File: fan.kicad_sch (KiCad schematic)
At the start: 10 parts, among them J2 Conn_01x02, J4 Conn_01x04, U7 EMC2101

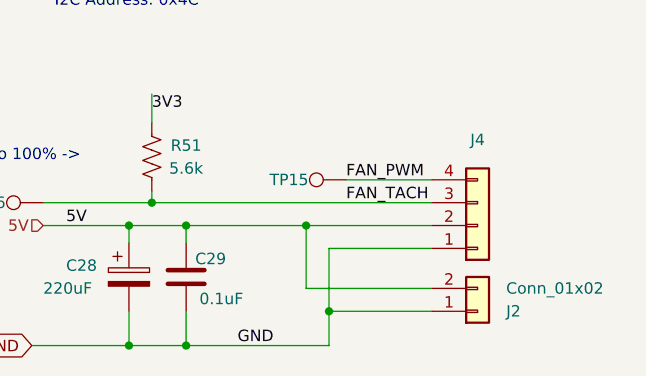
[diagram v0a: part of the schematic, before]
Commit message: Power analysis; updates to 205pd
Started analysis based on the 204 with an architecture diagram and with an smath document. Copied over manually changes from the 205 branch and started updating the schematic with USB PD capabilities. Only added decoy USB PD chip (CH224K), still need to fix power supplies.
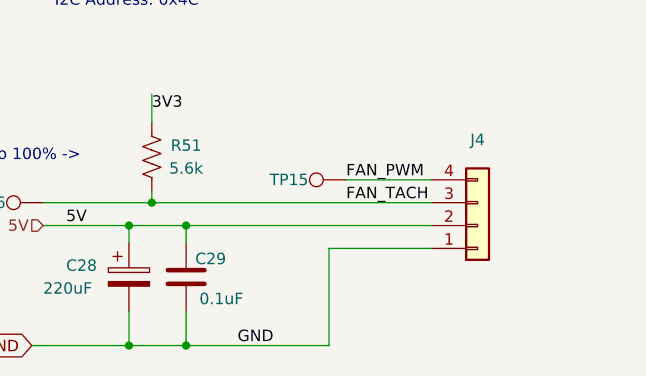
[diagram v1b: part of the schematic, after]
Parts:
- removed J2: Conn_01x02, bitaxe:JST_XH_B2B-XH-A_1x02_P2.50mm_Vertical, symbol Connector_Generic:Conn_01x02
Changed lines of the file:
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@@
   (title_block
     (title "Bitaxe Ultra")
-    (date "2023-12-10")
-    (rev "204")
+    (date "2023-12-15")
+    (rev "205")
   )
   (junction (at 191.77 66.04) (diameter 0) (color 0 0 0 0)
   )
-  (junction (at 164.465 113.665) (diameter 0) (color 0 0 0 0)
-  )
   (junction (at 151.13 113.665) (diameter 0) (color 0 0 0 0)
-  )
-  (junction (at 167.005 123.19) (diameter 0) (color 0 0 0 0)
   )
   (junction (at 147.32 111.125) (diameter 0) (color 0 0 0 0)
@@
     (stroke (width 0) (type default))
   )
-  (wire (pts (xy 164.465 120.65) (xy 178.435 120.65))
-    (stroke (width 0) (type default))
-  )
-  (wire (pts (xy 167.005 116.205) (xy 167.005 123.19))
-    (stroke (width 0) (type default))
-  )
   (wire (pts (xy 125.095 73.025) (xy 132.08 73.025))
     (stroke (width 0) (type default))
   )
-  (wire (pts (xy 167.005 123.19) (xy 167.005 127))
-    (stroke (width 0) (type default))
-  )
-  (wire (pts (xy 167.005 123.19) (xy 178.435 123.19))
+  (wire (pts (xy 167.005 116.205) (xy 167.005 127))
     (stroke (width 0) (type default))
   )
@@
     (stroke (width 0) (type default))
   )
-  (wire (pts (xy 164.465 113.665) (xy 178.435 113.665))
+  (wire (pts (xy 151.13 113.665) (xy 178.435 113.665))
     (stroke (width 0) (type default))
   )
@@
     (stroke (width 0) (type default))
   )
-  (wire (pts (xy 151.13 113.665) (xy 164.465 113.665))
-    (stroke (width 0) (type default))
-  )
   (wire (pts (xy 157.48 83.185) (xy 191.77 83.185))
     (stroke (width 0) (type default))
@@
   )
   (wire (pts (xy 133.985 127) (xy 144.78 127))
-    (stroke (width 0) (type default))
-  )
-  (wire (pts (xy 164.465 120.65) (xy 164.465 113.665))
     (stroke (width 0) (type default))
   )
@@
         )
       )
-    )
-  )
-  (symbol (lib_id "Connector_Generic:Conn_01x02") (at 183.515 123.19 0) (mirror x) (unit 1)
-    (in_bom yes) (on_board yes) (dnp no)
-    (property "Reference" "J2" (at 186.69 123.19 0)
-      (effects (font (size 1.27 1.27)) (justify left))
-    )
-    (property "Value" "Conn_01x02" (at 186.69 120.65 0)
-      (effects (font (size 1.27 1.27)) (justify left))
-    )
-    (property "Footprint" "bitaxe:JST_XH_B2B-XH-A_1x02_P2.50mm_Vertical" (at 183.515 123.19 0)
-      (effects (font (size 1.27 1.27)) hide)
-    )
-    (property "Datasheet" "https://www.jst-mfg.com/product/pdf/eng/eXH.pdf" (at 183.515 123.19 0)
-      (effects (font (size 1.27 1.27)) hide)
-    )
-    (property "DK" "455-B2B-XH-A-ND" (at 183.515 123.19 0)
-      (effects (font (size 1.27 1.27)) hide)
-    )
-    (property "PARTNO" "B2B-XH-A" (at 183.515 123.19 0)
-      (effects (font (size 1.27 1.27)) hide)
-    )
-    (pin "1")
-    (pin "2")
-    (instances
-      (project "bitaxeUltra"
-        (path "/e63e39d7-6ac0-4ffd-8aa3-1841a4541b55/8e8832ea-6bf1-49d2-b3a5-32a207f555d2"
-          (reference "J2") (unit 1)
-        )
-      )

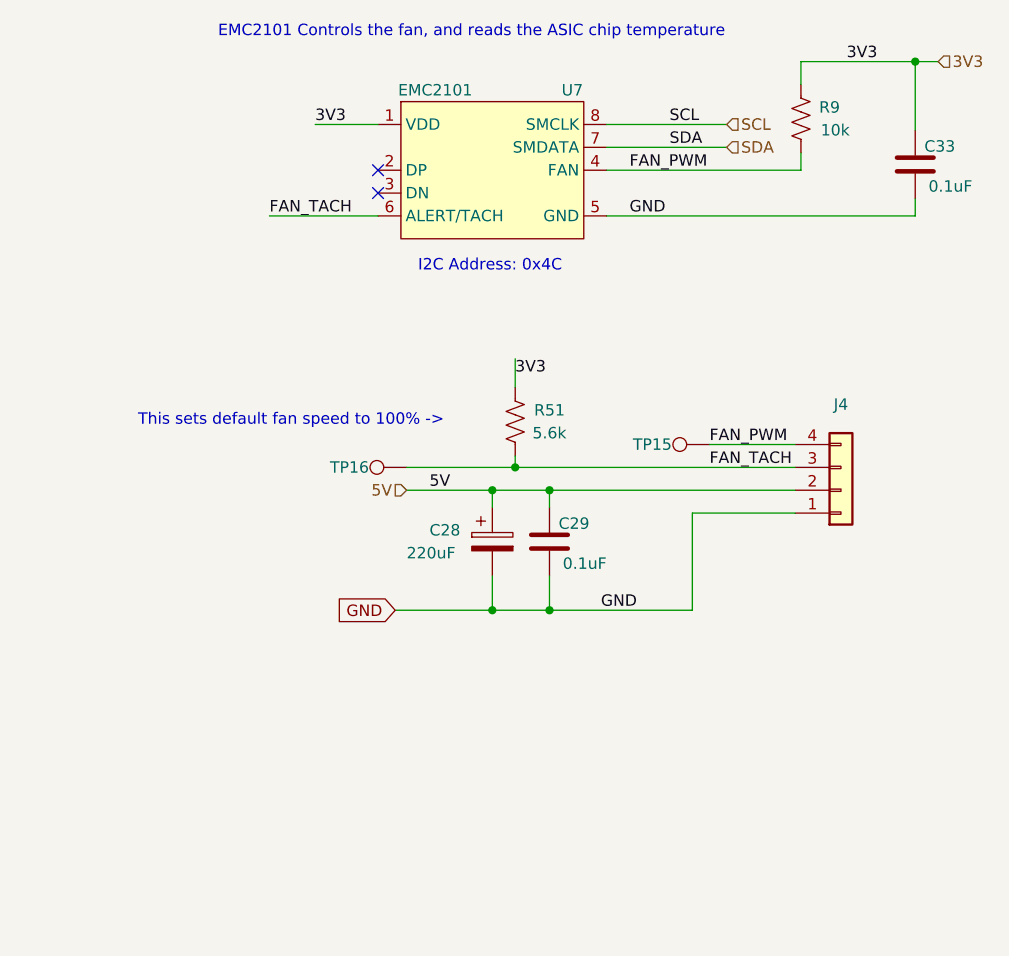
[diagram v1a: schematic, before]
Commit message: Worked on VDD
Started importing SiC431A for VDD supply. Yet to do Vfb, Mode, Pgood, boot, phase, en. Moved power supplies to power page. Configured CH224K to 12V
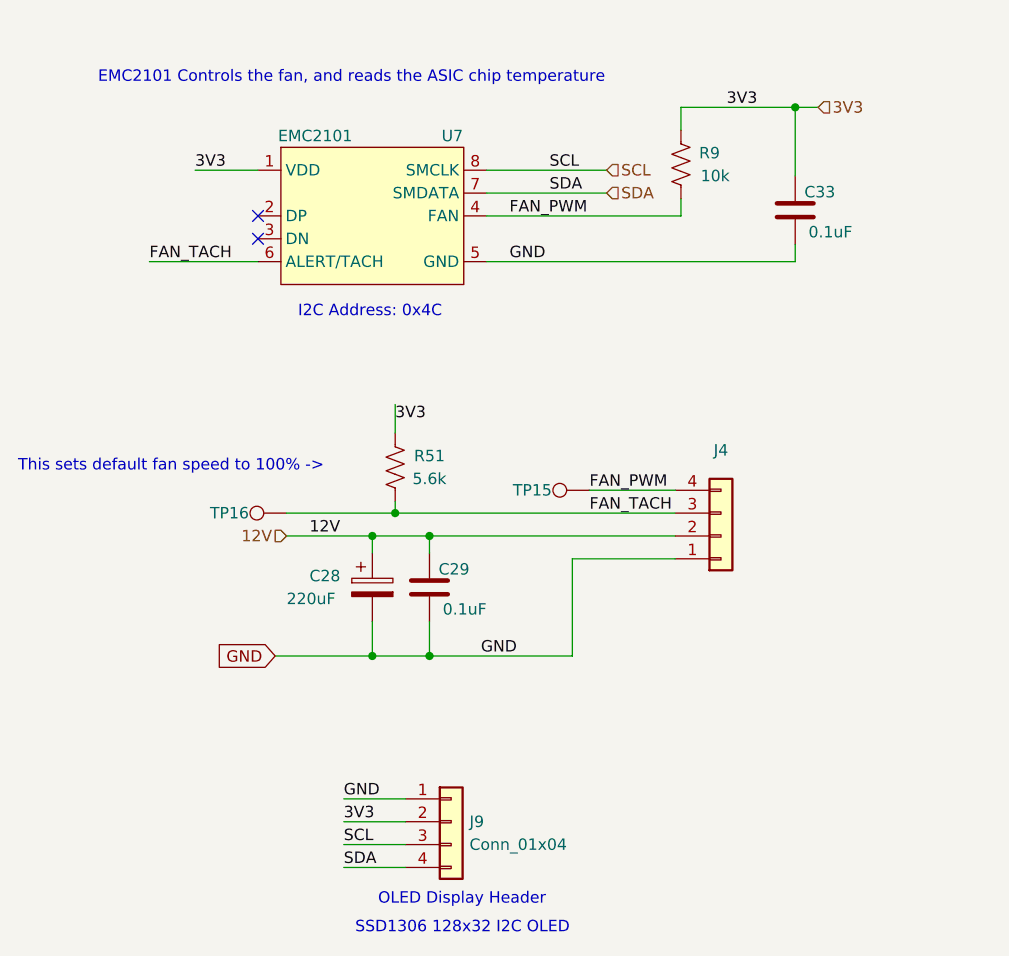
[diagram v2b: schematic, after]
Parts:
- added J9: Conn_01x04, bitaxe:PinHeader_1x04_P2.54mm_Vertical_shifted, symbol Connector_Generic:Conn_01x04
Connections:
- net 3V3: now also J9.2 (Pin_2)
- net GND: now also J9.1 (Pin_1)
- net SCL: now also J9.3 (Pin_3)
- net SDA: now also J9.4 (Pin_4)
- net 5V renamed 12V
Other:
- note added: "OLED Display Header"
- note added: "SSD1306 128x32 I2C OLED"
- moved on the sheet: C28, C29, C33, J4, R51, R9, TP15, TP16, U7

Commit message: SCH Draft 3, PCB Start
Finished some last minute changes to change 1V8 to 1V2 based on discord feedback. Updated level shifter and moved 25MHz oscillator to use 3V3 and be shifted down. Started working on layout.
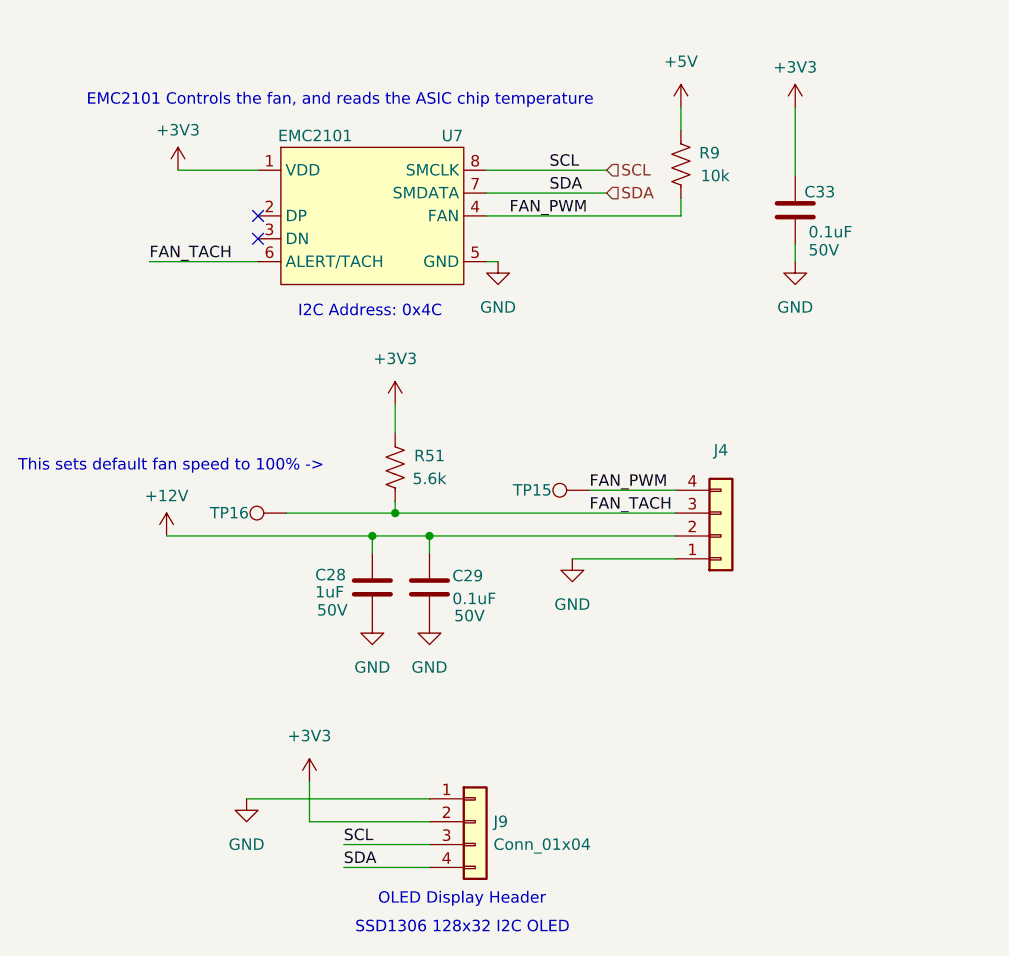
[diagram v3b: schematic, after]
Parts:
- removed C28: 220uF, Capacitor_SMD:CP_Elec_6.3x7.7, symbol Device:C_Polarized
- added C28: 1uF, Capacitor_SMD:C_0603_1608Metric, symbol Device:C
- C29, C33: DK 1292-1639-1-ND -> 490-13342-1-ND; PARTNO 0402X104K100CT -> GRM155R71H104KE14J; Voltage (none) -> 50V
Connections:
- net GND: now also C28.2
- net 12V renamed +12V
- net +12V: now also C28.1
- net 3V3 renamed +3V3
- net +3V3: no longer R9.2
- new net +5V: R9.2
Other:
- moved on the sheet: J9

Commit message: 3.3V net fix, PCB progress
Fixed accidental use of both 3V3 and 3.3V to just use 3V3. Worked on PCB
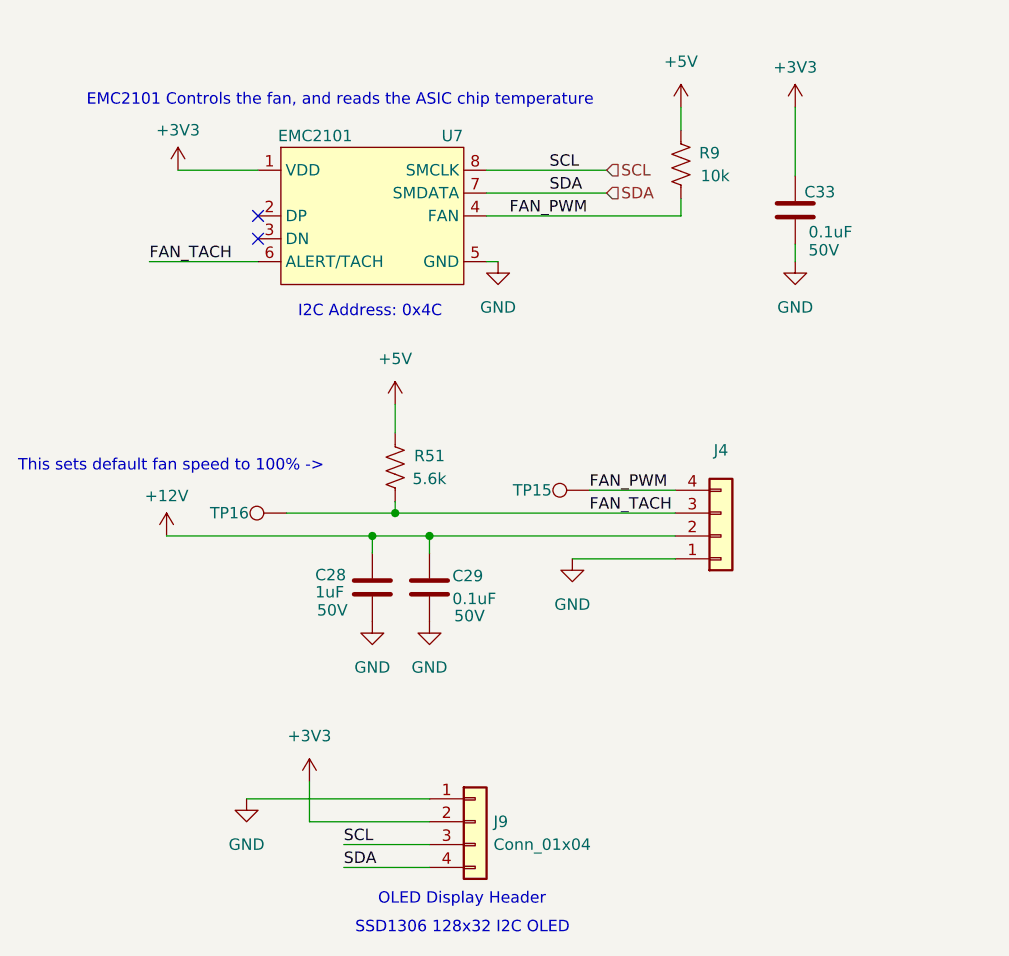
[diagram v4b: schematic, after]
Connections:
- net +3V3: no longer R51.2
- net +5V: now also R51.2
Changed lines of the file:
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@@
+    )
+  )
+  (symbol (lib_id "power:+5V") (at 133.985 104.14 0) (unit 1)
+    (in_bom yes) (on_board yes) (dnp no) (fields_autoplaced)
+    (property "Reference" "#PWR073" (at 133.985 107.95 0)
+      (effects (font (size 1.27 1.27)) hide)
+    )
+    (property "Value" "+5V" (at 133.985 99.06 0)
+      (effects (font (size 1.27 1.27)))
+    )
+    (property "Footprint" "" (at 133.985 104.14 0)
+      (effects (font (size 1.27 1.27)) hide)
+    )
+    (property "Datasheet" "" (at 133.985 104.14 0)
+      (effects (font (size 1.27 1.27)) hide)
+    )
+    (pin "1")
+    (instances
+      (project "bitaxeUltra"
+        (path "/e63e39d7-6ac0-4ffd-8aa3-1841a4541b55/8e8832ea-6bf1-49d2-b3a5-32a207f555d2"
+          (reference "#PWR073") (unit 1)
+        )
+      )
     )
   )
@@
         )
       )
-    )
-  )
-  (symbol (lib_id "power:+3V3") (at 133.985 104.14 0) (unit 1)
-    (in_bom yes) (on_board yes) (dnp no) (fields_autoplaced)
-    (property "Reference" "#PWR073" (at 133.985 107.95 0)
-      (effects (font (size 1.27 1.27)) hide)
-    )
-    (property "Value" "+3V3" (at 133.985 99.06 0)
-      (effects (font (size 1.27 1.27)))
-    )
-    (property "Footprint" "" (at 133.985 104.14 0)
-      (effects (font (size 1.27 1.27)) hide)
-    )
-    (property "Datasheet" "" (at 133.985 104.14 0)
-      (effects (font (size 1.27 1.27)) hide)
-    )
-    (pin "1")
-    (instances
-      (project "bitaxeUltra"
-        (path "/e63e39d7-6ac0-4ffd-8aa3-1841a4541b55/8e8832ea-6bf1-49d2-b3a5-32a207f555d2"
-          (reference "#PWR073") (unit 1)
-        )
-      )
